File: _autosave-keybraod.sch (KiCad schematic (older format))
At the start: 22 parts, among them J1 AVR-ISP-6, U1 ATmega32U4-AU, U2 PRTR5V0U2X, X1 XTAL

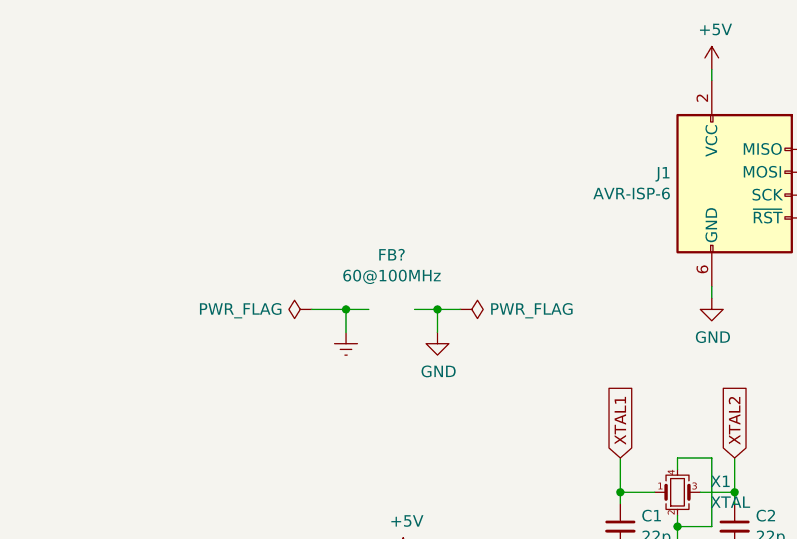
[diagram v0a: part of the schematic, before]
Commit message: part3 complete
-switch pcb mirror
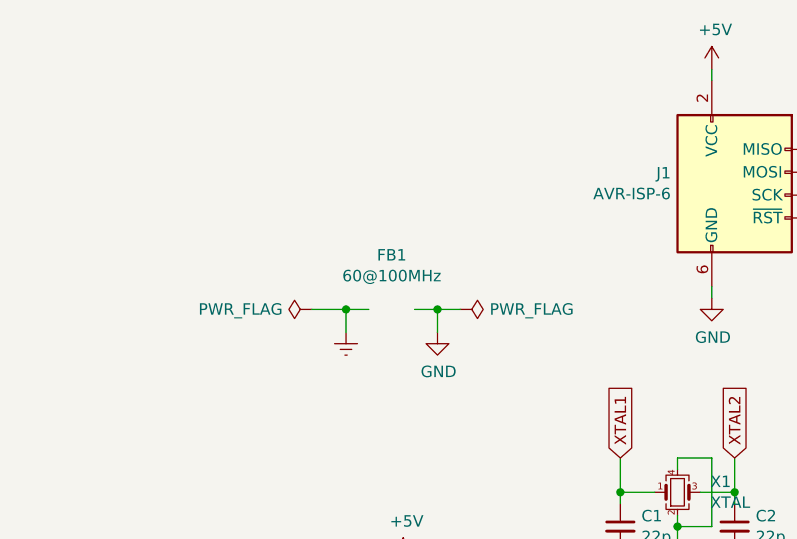
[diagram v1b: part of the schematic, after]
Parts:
- gave numbers to parts that had none: 1
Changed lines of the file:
@@
 row0
 $Comp
-L Device:Ferrite_Bead_Small FB?
-U 0 0 64959D2F
+L Device:Ferrite_Bead_Small FB1
+U 1 0 64959D2F
 P 4950 2100
-F 0 "FB?" V 4713 2100 50  0000 C CNN
+F 0 "FB1" V 4713 2100 50  0000 C CNN
 F 1 "60@100MHz" V 4804 2100 50  0000 C CNN
 F 2 "Inductor_SMD:L_0805_2012Metric_Pad1.15x1.40mm_HandSolder" V 4880 2100 50  0001 C CNN
 F 3 "~" H 4950 2100 50  0001 C CNN
-	0    4950 2100
+	1    4950 2100
 	0    1    1    0
 $EndComp
 $Comp
-L power:PWR_FLAG #FLG?
+L power:PWR_FLAG #FLG0101
 U 1 1 6495CA8D
 P 4600 2100
-F 0 "#FLG?" H 4600 2175 50  0001 C CNN
+F 0 "#FLG0101" H 4600 2175 50  0001 C CNN
 F 1 "PWR_FLAG" V 4600 2227 50  0000 L CNN
 F 2 "" H 4600 2100 50  0001 C CNN
@@
 $EndComp
 $Comp
-L power:PWR_FLAG #FLG?
+L power:PWR_FLAG #FLG0102
 U 1 1 6495CF9D
 P 5250 2100
-F 0 "#FLG?" H 5250 2175 50  0001 C CNN
+F 0 "#FLG0102" H 5250 2175 50  0001 C CNN
 F 1 "PWR_FLAG" V 5250 2228 50  0000 L CNN
 F 2 "" H 5250 2100 50  0001 C CNN
@@
 $EndComp
 $Comp
-L power:GND #PWR?
+L power:GND #PWR0101
 U 1 1 6495D132
 P 5150 2200
-F 0 "#PWR?" H 5150 1950 50  0001 C CNN
+F 0 "#PWR0101" H 5150 1950 50  0001 C CNN
 F 1 "GND" H 5155 2027 50  0000 C CNN
 F 2 "" H 5150 2200 50  0001 C CNN
@@
 $EndComp
 $Comp
-L power:Earth #PWR?
+L power:Earth #PWR0102
 U 1 1 6495D81C
 P 4750 2200
-F 0 "#PWR?" H 4750 1950 50  0001 C CNN
+F 0 "#PWR0102" H 4750 1950 50  0001 C CNN
 F 1 "Earth" H 4750 2050 50  0001 C CNN
 F 2 "" H 4750 2200 50  0001 C CNN
